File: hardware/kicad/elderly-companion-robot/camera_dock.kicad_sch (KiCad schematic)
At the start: 9 parts, among them J11 Servo_Pan, J12 Servo_Tilt, J13 IR_TX_LED, J14 IR_RX, J15 Dock_Contact, U9 SIM800C

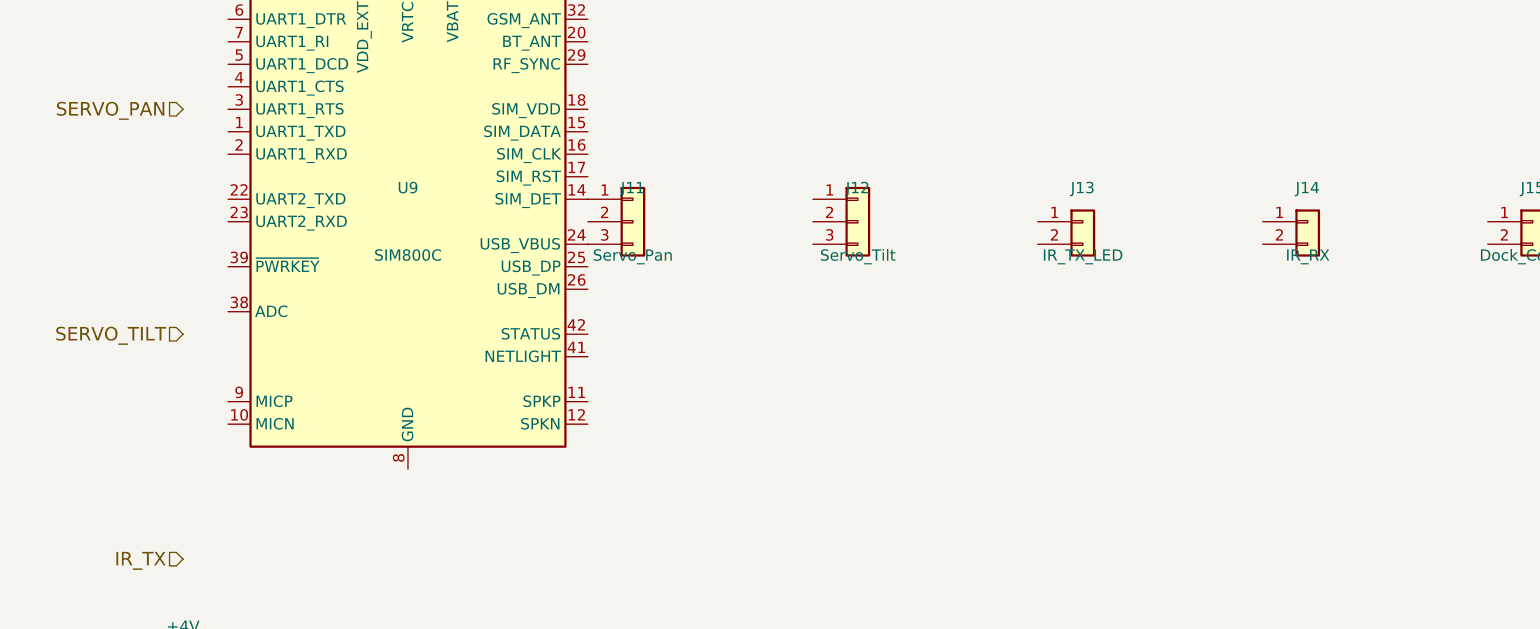
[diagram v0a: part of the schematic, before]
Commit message: Add net labels and signal connections across all schematic sheets
- MCU Core: Added net labels at all ESP32-S3 GPIO pin positions
  (I2C, I2S, motor, servo, IR, UART, ultrasonic signals)
- Added hierarchical labels for US_LEFT/RIGHT_TRIG/ECHO
- Remapped I2C_SCL to GPIO2 (GPIO22 not on WROOM-1 module)
- Remapped SERVO_PAN to GPIO42 (GPIO44 not available)
- Motor Driver: Added net labels at L298N input/output pins
- Sensors: Added I2C labels at MPU-6050 and SSD1306 pin positions
- Audio: Added I2S labels at MAX98357A and INMP441 connector
- Camera/Dock: Added UART, SIM_PWRKEY, servo, IR labels at SIM800C
- Added power symbols (+3V3, +5V, GND, +4V) across all sheets
- Boot circuit wiring started (EN pull-up, GPIO0 connections)
- ERC: 446 violations (mostly unconnected labels/pins - need wires)

Co-Authored-By: Claude Opus 4.7 <noreply@anthropic.com>
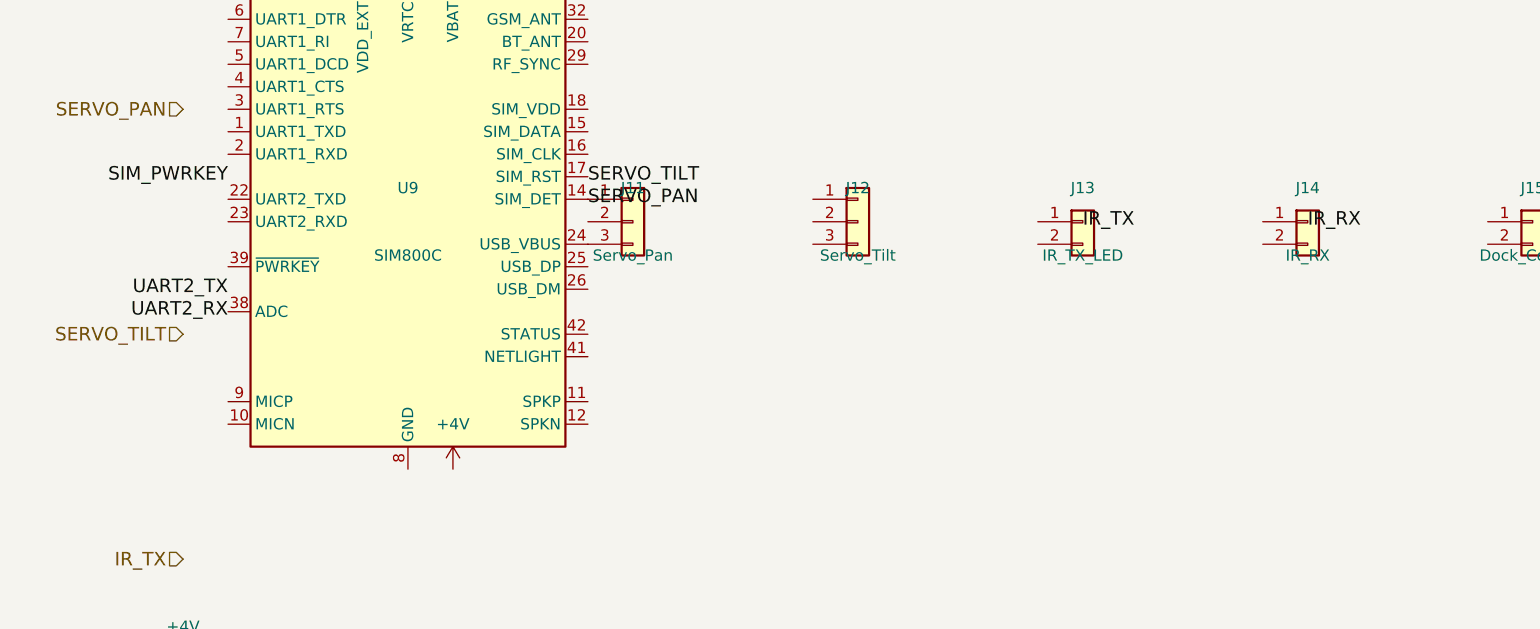
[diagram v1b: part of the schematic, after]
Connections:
- net SERVO_PAN: now also J11.1 (Pin_1), U9.14 (SIM_DET)
- net SERVO_TILT: now also U9.17 (SIM_RST)
- net UART2_RX: now also U9.38 (ADC)
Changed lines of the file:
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@@
 	(version 20250114)
 	(generator "eeschema")
+	(generator_version "9.0")
 	(paper "A4")
 	(symbol
@@
 		(effects (font (size 1.524 1.524)))
 	)
+	(label "UART2_RX"
+		(at 30.48 60.96 180)
+		(effects (font (size 1.524 1.524)))
+	)
+	(label "UART2_TX"
+		(at 30.48 58.42 180)
+		(effects (font (size 1.524 1.524)))
+	)
+	(label "SIM_PWRKEY"
+		(at 30.48 45.72 180)
+		(effects (font (size 1.524 1.524)))
+	)
+	(symbol
+		(lib_id "power:+4V")
+		(at 55.88 78.74 0)
+		(unit 1)
+		(exclude_from_sim no)
+		(in_bom yes)
+		(on_board yes)
+		(dnp no)
+		(property "Reference" "#PWR92f4"
+			(at 55.88 72.39 0)
+			(effects (font (size 1.27 1.27)) (hide yes))
+		)
+		(property "Value" "+4V"
+			(at 55.88 73.66 0)
+			(effects (font (size 1.27 1.27)))
+		)
+		(property "Footprint" ""
+			(at 55.88 78.74 0)
+			(effects (font (size 1.27 1.27)) (hide yes))
+		)
+		(property "Datasheet" "~"
+			(at 55.88 78.74 0)
+			(effects (font (size 1.27 1.27)) (hide yes))
+		)
+		(instances
+			(project "elderly-companion-robot"
+				(path "/55cdf11a-726b-4d96-98bb-530726b7b167"
+					(reference "#PWR92f4") (unit 1)
+				)
+			)
+		)
+	)
+	(label "SERVO_PAN"
+		(at 71.12 48.26 0)
+		(effects (font (size 1.524 1.524)))
+	)
+	(label "SERVO_TILT"
+		(at 71.12 45.72 0)
+		(effects (font (size 1.524 1.524)))
+	)
+	(label "IR_TX"
+		(at 127 50.8 0)
+		(effects (font (size 1.524 1.524)))
+	)
+	(label "IR_RX"
+		(at 152.4 50.8 0)
+		(effects (font (size 1.524 1.524)))
+	)
